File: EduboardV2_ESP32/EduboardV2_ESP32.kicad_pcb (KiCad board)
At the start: 4 copper layers, 35 x 63.3 mm, 89 parts, among them J1 EduboardV2 PCIE UP Board Conn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, Q1 S8050_C139514, Q2 S8050_C139514, Q3 AO3401A, SW1 K2-1102SP-C4SC-04, SW2 K2-1102SP-C4SC-04, U1 ESP32-WROOM-E, U2 FT2232HL, U3 M93C46-WMN6TP, U4 SX1509BIULTRT, U5 LD1117S33TR_SOT223, Y2 12MHz

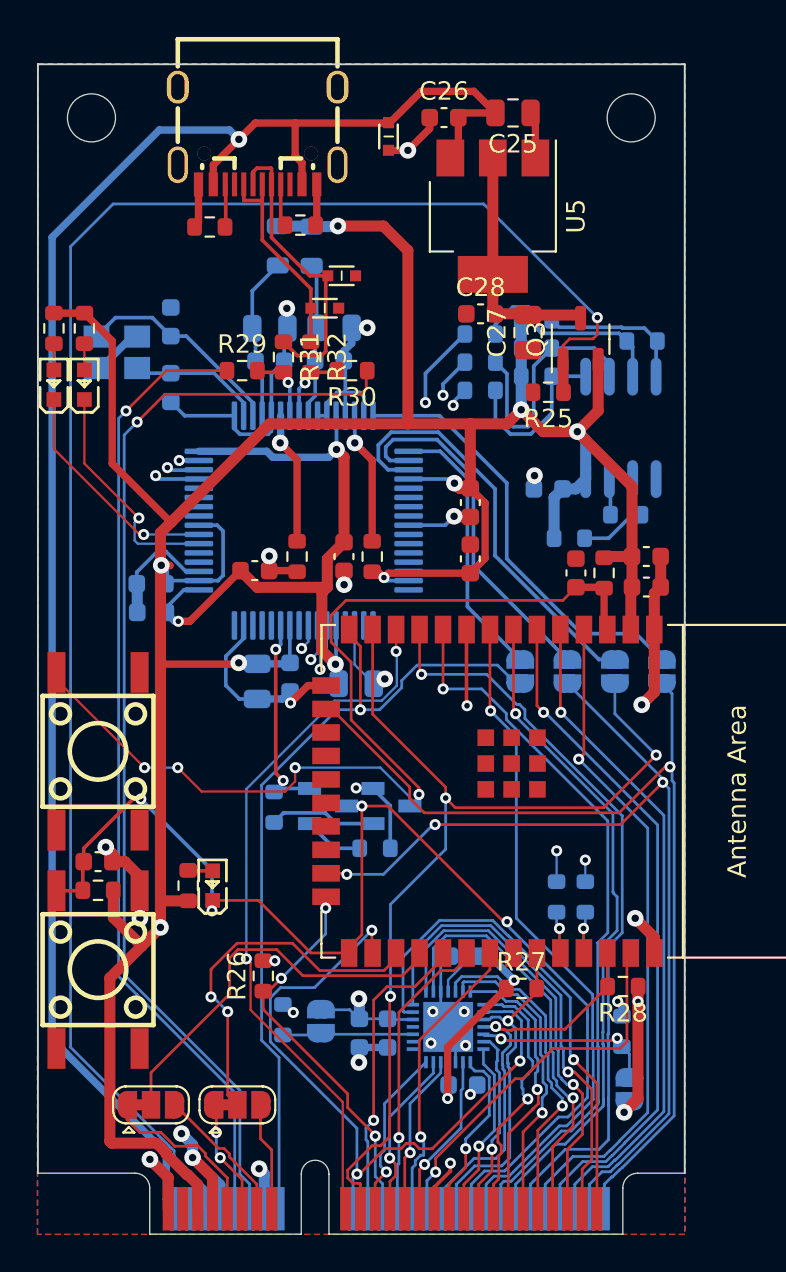
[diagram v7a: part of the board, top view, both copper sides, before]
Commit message: finalize Layout, fill in most of the critical part info. Replace certain parts with Eduboard kicadlib Parts.
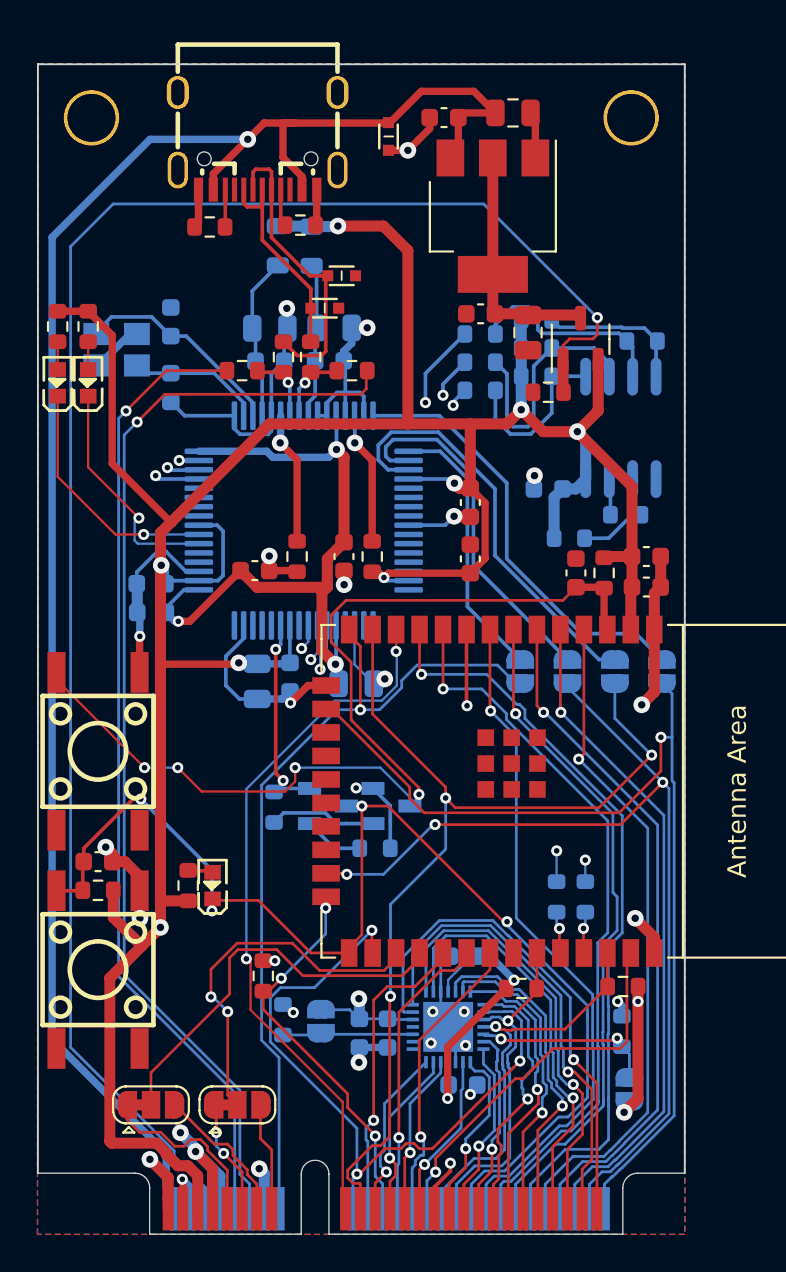
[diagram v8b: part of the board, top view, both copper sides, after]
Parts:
- LED1, LED2, LED3: footprint JLCPCB:LED0603-RD -> EduboardV2_kicadlib:LED0603-FD_BLUE
- Q1, Q2: footprint JLCPCB:SOT-23-3_L2.9-W1.3-P1.90-LS2.4-BR -> EduboardV2_kicadlib:SOT-23-3_L2.9-W1.3-P1.90-LS2.4-BR
- SW1, SW2: footprint JLCPCB:KEY-SMD_4P-L6.0-W6.0-P4.50-LS9.5-BL -> EduboardV2_kicadlib:KEY-SMD_4P-L6.0-W6.0-P4.50-LS9.5-BL
- U3: footprint JLCPCB:SOIC-8_L4.9-W3.9-P1.27-LS6.0-BL -> EduboardV2_kicadlib:SOIC-8_L4.9-W3.9-P1.27-LS6.0-BL
- USBC1: footprint JLCPCB:USB-C-SMD_TYPE-C-USB-17 -> EduboardV2_kicadlib:USB-C-SMD_TYPE-C-USB-17
- moved USBC1 0.29 mm to (112.4, 98.3)
- moved LED1 0.23 mm to (103.3, 111.4)
- moved R13 0.23 mm to (103.3, 108.3)
- moved LED2 0.23 mm to (101.6, 111.4)
- moved R14 0.23 mm to (101.6, 108.3)
- moved Y2 0.14 mm to (104.8, 109.6)
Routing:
- net GND: track 111.9 -> 115.6 mm, vias 26 -> 27
- net +5V: track 0.00 -> 3.39 mm, vias 0 -> 1
- net ESP_TCK: track 52.6 -> 54.5 mm
- net Net-(LED2-C): track 12.4 -> 13.2 mm
- net VBUS: track 94.5 -> 95.2 mm
- net Net-(J1-UART0_UP_TX): track 9.32 -> 9.87 mm
- net D+: track 11.5 -> 12.0 mm
